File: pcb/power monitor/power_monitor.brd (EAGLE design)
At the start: 22.9 x 30.5 mm, 17 parts, among them IC1 MAX4105ESA, IC2 MAX4105ESA, IC3 MAX4105ESA

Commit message: Signed-off-by: timcronin <tmpcronin@gmail.com>
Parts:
- removed C6: 100 nF, rcl:C0402
- removed R5, R6: 500K, rcl:R0603
- moved IC1 0.22 mm to (3.61, 24.8), turned to 180 degrees
- turned IC3 to 180 degrees
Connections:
- removed net N$5: C6.1, R5.1, R6.2, U$5.3
- new net N$2: IC3.6, R3.1, U$5.3
- net DAT: no longer IC3.6, R3.1
- net GND: no longer C6.2, R6.1
- net V+: no longer R5.2
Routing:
- net N$4: track 19.8 -> 45.8 mm
- net N$5: track 22.0 -> 0.00 mm, vias 2 -> 0
- net N$2: track 0.00 -> 21.0 mm, vias 0 -> 2
- net DAT: track 39.9 -> 19.6 mm
- net N$11: track 44.0 -> 28.6 mm, vias 4 -> 2
- net N$9: track 12.6 -> 23.3 mm
- net GND: track 77.9 -> 87.7 mm, vias 5 -> 4
- net N$1: track 31.6 -> 24.1 mm, vias 3 -> 2
- net N$3: track 21.8 -> 29.1 mm, vias 2 -> 3
- net N$7: track 7.32 -> 14.6 mm, vias 0 -> 2
- net IRQ: track 21.3 -> 23.9 mm
- net V+: track 47.6 -> 49.8 mm
- net VCCINT: track 61.4 -> 63.3 mm
- net N$8: track 12.4 -> 10.6 mm, vias 1 -> 0
- net CLK: track 30.1 -> 31.7 mm

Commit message: Signed-off-by: timcronin <tmpcronin@gmail.com>
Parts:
- removed IC1, IC2, IC3: MAX4105ESA, maxim:SO08
- removed R7: 1k, rcl:R0603
- removed R8: 69.8k, rcl:R0603
- added C2: 10 uF, rcl:C0805
- added C3: 10 nF, rcl:C0402
- added C4: 22 uF, rcl:C1206
- added C5: 22 uF, rcl:C0402
- added C6: 100 nF, rcl:C0402
- added J1: (no value), con-jack:DCJ0303
- added R5, R6: 500K, rcl:R0603
- added U$1: MOMO-EDGE-SMALL-M, components:MOMO-EDGE-SMALL-6M
- added U$2: MOMO-EDGE-SMALL-F, components:MOMO-EDGE-SMALL-6F
- added U$3: MOMO-EDGE-POWER-M, components:MOMO-EDGE-SMALL-2M
- added U$4: MOMO-EDGE-POWER-F, components:MOMO-EDGE-SMALL-2F
- added U$8: 4.7 uH, components:NR6028-INDUCTOR
- added U$9: MCP1702, components:SOT23
- R2: value 2 -> 100K
- R3: value 69.8k -> 50K 1%
- R4: value 1k -> 13K 1%
- U$6: value MOMO-EDGE-8F -> XRP7659; device components:MOMO-EDGE-8F -> components:SOT23-6L
- U$7: value MOMO-EDGE-8M -> DIODE_SS2P3; device components:MOMO-EDGE-8M -> components:DIODE_SS2P3
- moved R1 13.4 mm to (8.36, 7.11), turned to 270 degrees
- moved U$6 13.4 mm to (11.4, 19.8), turned to 90 degrees
- moved C1 11.3 mm to (5.84, 8.00), turned to 180 degrees
- moved R4 10.2 mm to (16.0, 23.0), turned to 270 degrees
- moved R2 8.77 mm to (4.93, 19.5), turned to 180 degrees
- moved U$7 8.14 mm to (10.8, 10.1)
- moved U$5 7.03 mm to (4.47, 11.2), turned to 90 degrees
- moved R3 5.94 mm to (16.0, 19.9), turned to 270 degrees
- moved JP1 3.09 mm to (8.46, 2.01), turned to 180 degrees
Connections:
- removed net N$11: IC2.3, R2.1, U$7.V28
- removed net N$7: IC3.2, R3.2, R4.1
- removed net N$9: IC3.3, R7.1, R8.2
- new net +12V: C2.1, J1.1, R2.1, U$6.5
- new net N$5: C6.1, R5.1, R6.2, U$5.3
- new net N$6: R3.1, R4.2, U$6.3
- new net NC: U$1.2, U$2.2
- net CLK: now also U$1.3, U$2.3; no longer U$6.CLK, U$7.CLK
- net DAT: now also U$1.4, U$2.4; no longer U$6.DAT, U$7.DAT
- net GND: now also C2.2, C4.2, C5.2, C6.2, J1.2, J1.3, R4.1, R6.1, U$1.6, U$2.6, U$3.2, U$4.2, U$6.2, U$7.AN, U$9.1; no longer IC1.4, IC2.4, IC3.4, R8.1, U$6.GND, U$6.PGND, U$7.GND, U$7.PGND
- net IRQ: now also U$1.5, U$2.5; no longer U$6.ARLM, U$7.ALRM
- net N$2: now also C3.2, U$6.6, U$7.CATH, U$8.1; no longer IC3.6, R3.1, U$5.3
- net N$3: now also R2.2, U$6.4; no longer IC2.2, IC2.6, R4.2
- net N$4: now also C3.1, U$6.1; no longer IC1.2, IC1.6, R7.2
- net V+: now also C4.1, R3.2, R5.2, U$3.1, U$4.1, U$8.2, U$9.3; no longer IC3.7, U$6.V4., U$7.V4
- net VCCINT: now also C5.1, U$1.1, U$2.1, U$9.2; no longer IC1.3, IC1.7, IC2.7, R2.2, U$6.V28
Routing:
- net GND: track 87.7 -> 129.5 mm, vias 4 -> 16
- net N$4: track 45.8 -> 12.0 mm, vias 2 -> 0
- net N$11: track 28.6 -> 0.00 mm, vias 2 -> 0
- net N$9: track 23.3 -> 0.00 mm, vias 2 -> 0
- net NC: track 0.00 -> 22.0 mm
- net IRQ: track 23.9 -> 44.9 mm
- net CLK: track 31.7 -> 51.7 mm, vias 1 -> 0
- net N$3: track 29.1 -> 14.4 mm, vias 3 -> 0
- net N$7: track 14.6 -> 0.00 mm, vias 2 -> 0
- net DAT: track 19.6 -> 32.4 mm
- net N$5: track 0.00 -> 9.44 mm
- net +12V: track 0.00 -> 7.81 mm
- net VCCINT: track 63.3 -> 70.9 mm, vias 4 -> 2
- net N$6: track 0.00 -> 5.24 mm
- net N$8: track 10.6 -> 14.9 mm
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- added copper zone on layer 1, net +12V
- added copper zone on layer 1, net GND
- added copper zone on layer 16, net GND
- added copper zone on layer 1, net N$2
- added copper zone on layer 1, net V+
- added copper zone on layer 16, net V+
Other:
- board size 22.9 x 30.5 mm -> 7 x 7.1 mm
- board text added: "L1"
- board text added: "Prog"

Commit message: Signed-off-by: timcronin <tmpcronin@gmail.com>
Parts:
- removed C2: 10 uF, rcl:C0805
- removed C3: 10 nF, rcl:C0402
- removed C4: 22 uF, rcl:C1206
- removed C5: 22 uF, rcl:C0402
- removed C6: 100 nF, rcl:C0402
- removed J1: (no value), con-jack:DCJ0303
- removed R1: 10K, rcl:R0603
- removed R5, R6: 500K, rcl:R0603
- removed U$1: MOMO-EDGE-SMALL-M, components:MOMO-EDGE-SMALL-6M
- removed U$2: MOMO-EDGE-SMALL-F, components:MOMO-EDGE-SMALL-6F
- removed U$3: MOMO-EDGE-POWER-M, components:MOMO-EDGE-SMALL-2M
- removed U$4: MOMO-EDGE-POWER-F, components:MOMO-EDGE-SMALL-2F
- removed U$8: 4.7 uH, components:NR6028-INDUCTOR
- removed U$9: MCP1702, components:SOT23
- added IC1, IC2, IC3: MAX4105ESA, maxim:SO08
- added R7: 1k, rcl:R0603
- added R8: 69.8k, rcl:R0603
- R2: value 100K -> 2
- R3: value 50K 1% -> 69.8k
- R4: value 13K 1% -> 1k
- U$6: value XRP7659 -> MOMO-EDGE-8F; device components:SOT23-6L -> components:MOMO-EDGE-8F
- U$7: value DIODE_SS2P3 -> MOMO-EDGE-8M; device components:DIODE_SS2P3 -> components:MOMO-EDGE-8M
- moved JP1 32.3 mm to (40.8, 2.16)
- moved C1 28.5 mm to (34.3, 6.22), turned to 270 degrees
- moved U$6 28.4 mm to (39.8, 19.1), turned to 0 degrees
- moved U$5 24.8 mm to (29.3, 10.8), turned to 180 degrees
- moved R3 19.4 mm to (24.9, 2.72), turned to 90 degrees
- moved R4 18.7 mm to (24.9, 6.65), turned to 90 degrees
- moved R2 16.5 mm to (20.8, 23.9), turned to 0 degrees
- moved U$7 11.3 mm to (3.78, 18.9)
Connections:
- removed net +12V: C2.1, J1.1, R2.1, U$6.5
- removed net N$5: C6.1, R5.1, R6.2, U$5.3
- removed net N$6: R3.1, R4.2, U$6.3
- removed net NC: U$1.2, U$2.2
- new net N$11: IC2.3, R2.1, U$7.V28
- new net N$7: IC3.2, R3.2, R4.1
- new net N$9: IC3.3, R7.1, R8.2
- net CLK: now also U$6.CLK, U$7.CLK; no longer U$1.3, U$2.3
- net DAT: now also U$6.DAT, U$7.DAT; no longer U$1.4, U$2.4
- net GND: now also IC1.4, IC2.4, IC3.4, R8.1, U$6.GND, U$6.PGND, U$7.GND, U$7.PGND; no longer C2.2, C4.2, C5.2, C6.2, J1.2, J1.3, R4.1, R6.1, U$1.6, U$2.6, U$3.2, U$4.2, U$6.2, U$7.AN, U$9.1
- net IRQ: now also U$6.ARLM, U$7.ALRM; no longer U$1.5, U$2.5
- net N$1: now also U$6.NV, U$7.NC; no longer R1.2
- net N$2: now also IC3.6, R3.1, U$5.3; no longer C3.2, U$6.6, U$7.CATH, U$8.1
- net N$3: now also IC2.2, IC2.6, R4.2; no longer R2.2, U$6.4
- net N$4: now also IC1.2, IC1.6, R7.2; no longer C3.1, U$6.1
- net V+: now also IC3.7, U$6.V4., U$7.V4; no longer C4.1, R3.2, R5.2, U$3.1, U$4.1, U$8.2, U$9.3
- net VCCINT: now also IC1.3, IC1.7, IC2.7, R2.2, U$6.V28; no longer C5.1, R1.1, U$1.1, U$2.1, U$9.2
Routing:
- net N$1: track 20.5 -> 92.3 mm, vias 2 -> 4
- net N$4: track 12.0 -> 58.4 mm, vias 0 -> 4
- net CLK: track 51.7 -> 88.4 mm, vias 0 -> 3
- net DAT: track 32.4 -> 61.2 mm, vias 1 -> 4
- net N$3: track 14.4 -> 39.7 mm, vias 0 -> 3
- net N$11: track 0.00 -> 24.5 mm
- net NC: track 22.0 -> 0.00 mm
- net N$7: track 0.00 -> 20.3 mm, vias 0 -> 2
- net N$2: track 18.1 -> 29.2 mm, vias 0 -> 2
- net GND: track 129.5 -> 139.4 mm, vias 16 -> 6
- net N$5: track 9.44 -> 0.00 mm
- net N$9: track 0.00 -> 8.52 mm
- net IRQ: track 44.9 -> 52.7 mm, vias 1 -> 0
- net +12V: track 7.81 -> 0.00 mm
- net N$6: track 5.24 -> 0.00 mm
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- added copper zone on layer 16, net N$5
- removed copper zone on layer 1, net +12V
- removed copper zone on layer 1, net GND
- removed copper zone on layer 16, net GND
- removed copper zone on layer 1, net N$2
- removed copper zone on layer 1, net V+
- removed copper zone on layer 16, net V+
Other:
- board size 7 x 7.1 mm -> 46.3 x 30.5 mm
- board text removed: "L1"
- board text removed: "Prog"

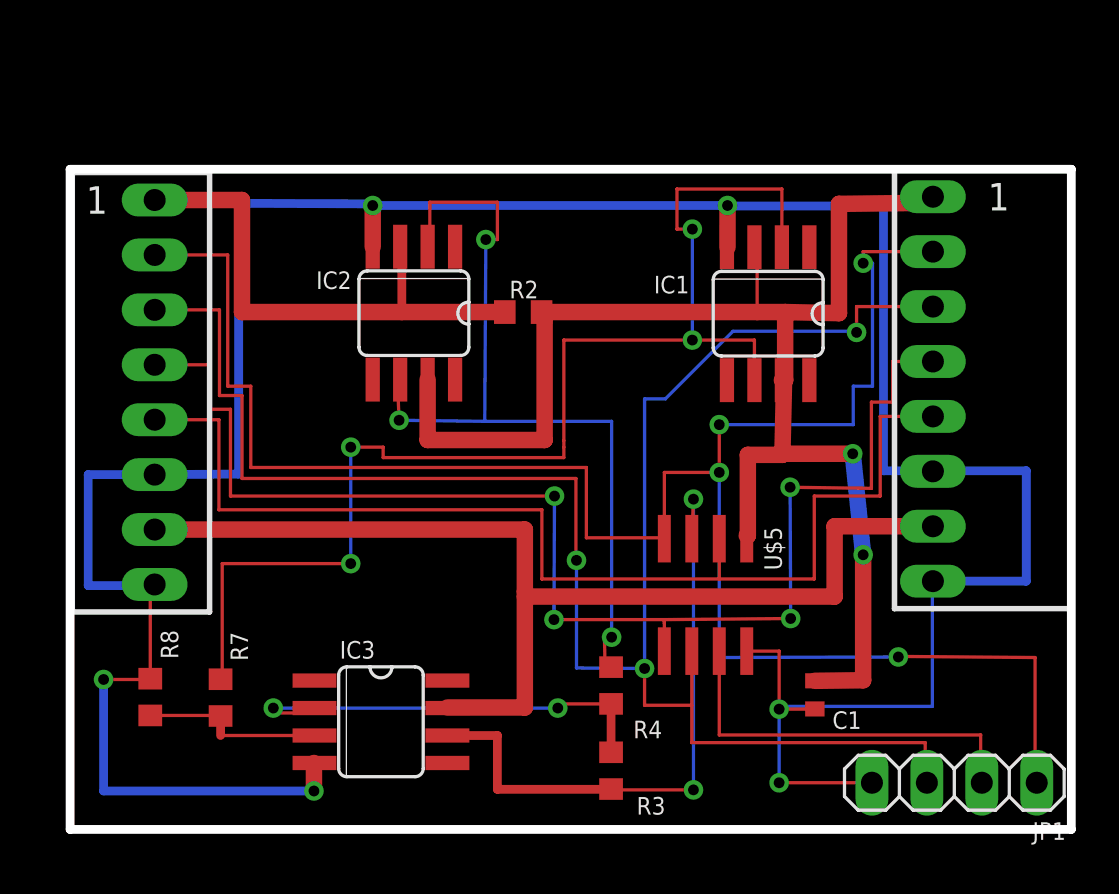
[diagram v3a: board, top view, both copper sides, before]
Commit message: Increased width of ground lines
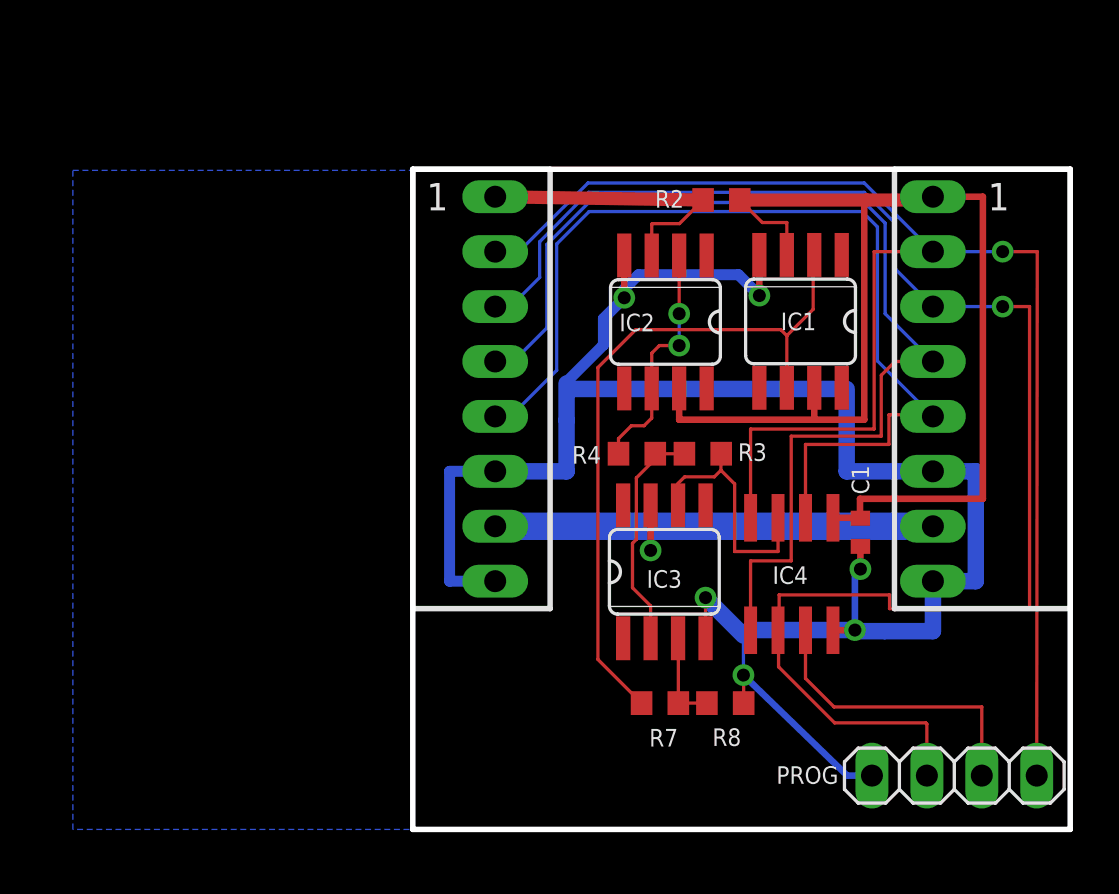
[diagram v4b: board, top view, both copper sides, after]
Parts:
- removed JP1: (no value), pinhead:1X04
- removed U$5: PIC12LF1822, components:SOIC8
- added IC4: PIC12LF1822, components:SOIC8
- added PROG: (no value), pinhead:1X04
- moved R8 26.6 mm to (30.2, 5.84), turned to 180 degrees
- moved R7 20.3 mm to (27.2, 5.84), turned to 180 degrees
- moved U$7 15.7 mm to (19.5, 19.1)
- moved R3 15.3 mm to (29.1, 17.4), turned to 180 degrees
- moved IC3 14.8 mm to (27.4, 11.9), turned to 0 degrees
- moved IC2 11.6 mm to (27.4, 23.5)
- moved R4 10.8 mm to (26.1, 17.4), turned to 180 degrees
- moved R2 10.5 mm to (30.0, 29.1)
- moved C1 7.81 mm to (36.4, 13.7)
- moved IC1 1.54 mm to (33.7, 23.5)
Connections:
- net CLK: now also IC4.6, PROG.3; no longer JP1.3, U$5.6
- net DAT: now also IC4.5; no longer U$5.5
- net GND: now also IC4.8, PROG.4; no longer JP1.4, U$5.8
- net IRQ: now also IC4.2; no longer U$5.2
- net N$1: now also IC4.4, PROG.1; no longer JP1.1, U$5.4
- net N$2: now also IC4.3; no longer U$5.3
- net N$8: now also IC4.7, PROG.2; no longer JP1.2, U$5.7
- net VCCINT: now also IC4.1; no longer U$5.1
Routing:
- net GND: track 139.4 -> 94.4 mm
- net N$3: track 39.7 -> 11.2 mm, vias 3 -> 2
- net V+: track 51.3 -> 23.4 mm, vias 0 -> 1
- net N$4: track 58.4 -> 32.6 mm, vias 4 -> 0
- net N$1: track 92.3 -> 72.9 mm, vias 4 -> 1
- net N$2: track 29.2 -> 11.6 mm, vias 2 -> 0
- net CLK: track 88.4 -> 71.2 mm, vias 3 -> 1
- net N$11: track 24.5 -> 13.9 mm
- net VCCINT: track 69.1 -> 59.0 mm, vias 2 -> 0
- net DAT: track 61.2 -> 51.5 mm, vias 4 -> 0
- net N$7: track 20.3 -> 10.8 mm, vias 2 -> 0
- net IRQ: track 52.7 -> 45.9 mm
- net N$9: track 8.52 -> 4.32 mm
- net N$8: track 18.2 -> 14.1 mm
- added copper zone on layer 16, net GND
- removed copper zone on layer 16, net N$5
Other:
- board size 46.3 x 30.5 mm -> 30.4 x 30.5 mm
